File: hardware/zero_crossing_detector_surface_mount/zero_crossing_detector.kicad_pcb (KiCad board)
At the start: 2 copper layers, 93 x 61 mm, 98 parts, among them J1 Conn_01x02, J2 BOOT0, J3 Conn_02x15_Odd_Even, J4 USB_B_Micro, J6 K-Type, J7 BOOT1, Q1 2N3904, Q2 2N3904, Q3 2N3904, SW1 Reset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

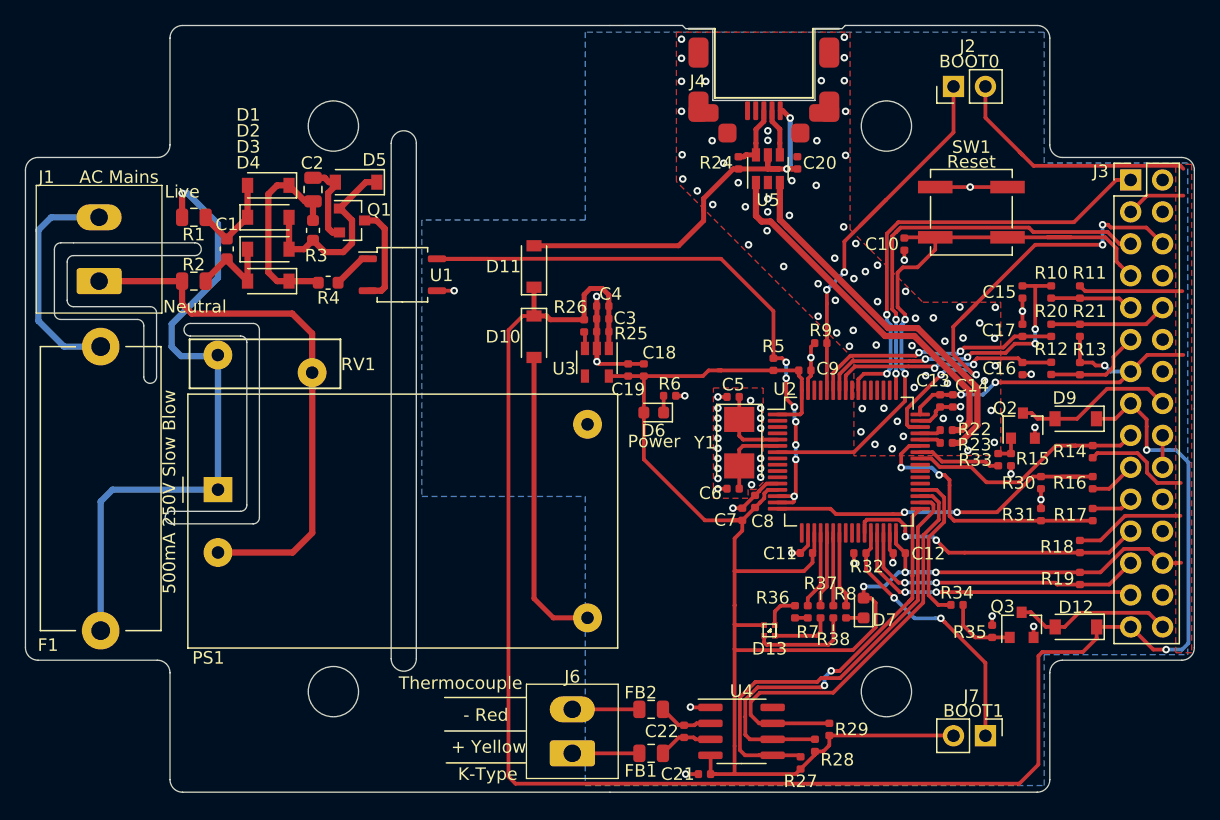
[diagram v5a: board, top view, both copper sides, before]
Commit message: Tweaked solder mask expansion
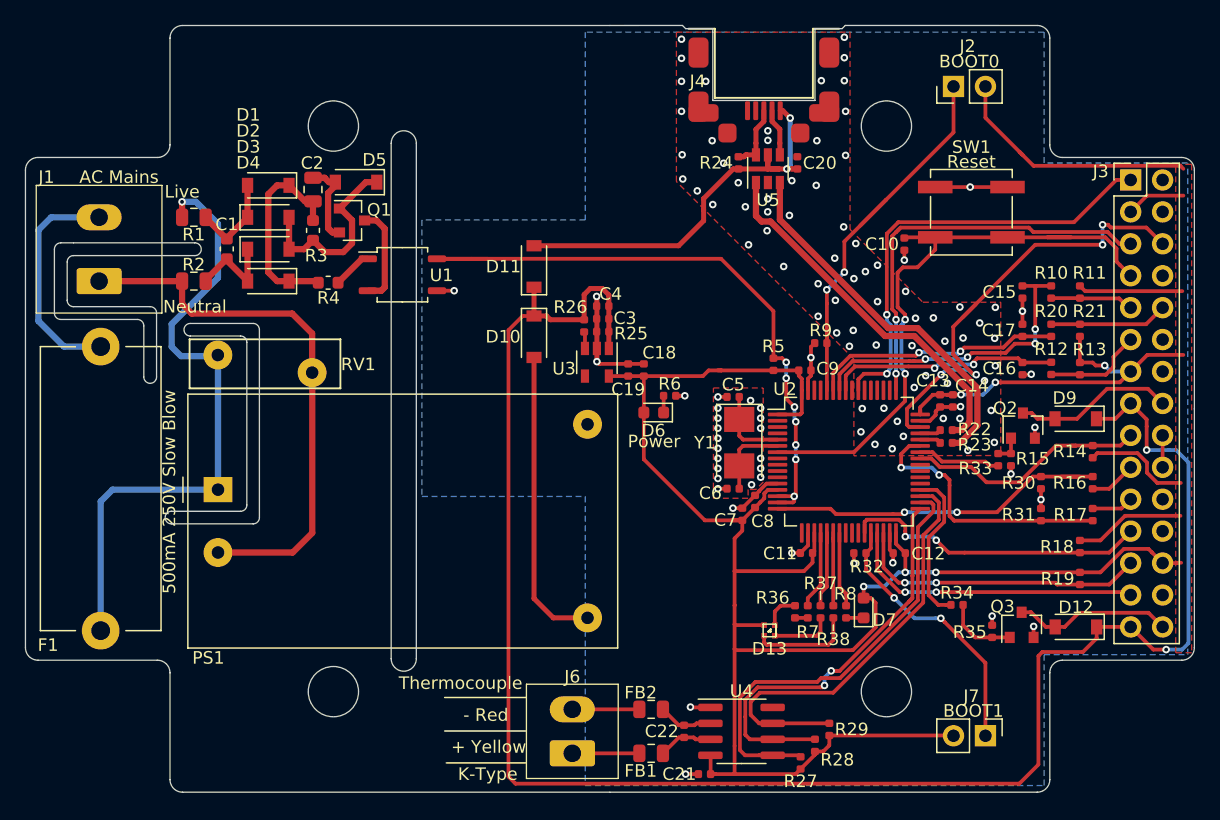
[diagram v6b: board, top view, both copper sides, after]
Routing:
- net /Fused_LIVE: track 51.7 -> 50.7 mm
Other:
- rule solder_mask_min_width: 0.25 -> 0.1
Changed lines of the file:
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@@
     (thickness 1.6)
     (drawings 147)
-    (tracks 912)
+    (tracks 913)
     (zones 0)
     (modules 98)
@@
   )
   (setup
-    (last_trace_width 0.4)
+    (last_trace_width 0.127)
     (user_trace_width 0.3)
     (user_trace_width 0.4)
@@
     (pad_drill 1)
     (pad_to_mask_clearance 0.051)
-    (solder_mask_min_width 0.25)
+    (solder_mask_min_width 0.1)
     (aux_axis_origin 0 0)
     (visible_elements FFFFFF7F)
@@
     (tags resistor)
     (attr smd)
-    (fp_text reference R33 (at 0.023 1.8288 180) (layer F.SilkS)
+    (fp_text reference R33 (at 0.6961 1.8161 180) (layer F.SilkS)
       (effects (font (size 1 1) (thickness 0.15)))
     )
@@
     (tags capacitor)
     (attr smd)
-    (fp_text reference C21 (at 2.136 0) (layer F.SilkS)
+    (fp_text reference C21 (at 2.009 0) (layer F.SilkS)
       (effects (font (size 1 1) (thickness 0.15)))
     )
@@
     (pad "" np_thru_hole circle (at 0 0) (size 4 4) (drill 4) (layers *.Cu *.Mask))
   )
+  (gr_text Live (at 175.964 52.728) (layer F.SilkS)
+    (effects (font (size 1 1) (thickness 0.15)))
+  )
   (gr_line (start 226.7585 85.1535) (end 226.7585 84.5185) (layer F.SilkS) (width 0.12))
   (gr_line (start 227.7745 87.63) (end 227.7745 87.1855) (layer F.SilkS) (width 0.12))
@@
     (effects (font (size 1 1) (thickness 0.15)))
   )
-  (gr_text Live (at 175.964 52.728) (layer F.SilkS)
-    (effects (font (size 1 1) (thickness 0.15)))
-  )
   (gr_arc (start 176 40.5) (end 176 39.5) (angle -90) (layer Edge.Cuts) (width 0.05))
   (gr_arc (start 174 49) (end 174 50) (angle -90) (layer Edge.Cuts) (width 0.05))
@@
     (effects (font (size 1.2 1.2) (thickness 0.2)) (justify mirror))
   )
-  (via (at 222.5675 48.641) (size 0.6) (drill 0.3) (layers F.Cu B.Cu) (net 5))
-  (via (at 222.5675 47.879) (size 0.6) (drill 0.3) (layers F.Cu B.Cu) (net 5))
-  (via (at 236.855 67.9704) (size 0.6) (drill 0.3) (layers F.Cu B.Cu) (net 5))
   (segment (start 177.839 54.806) (end 179.52 56.487) (width 0.5) (layer F.Cu) (net 1))
   (segment (start 177.839 54.76) (end 177.839 54.806) (width 0.5) (layer F.Cu) (net 1))
@@
   (segment (start 187.917 55.964) (end 187.579 55.626) (width 0.5) (layer F.Cu) (net 4))
   (segment (start 188.484 55.964) (end 187.917 55.964) (width 0.5) (layer F.Cu) (net 4))
+  (via (at 222.5675 48.641) (size 0.6) (drill 0.3) (layers F.Cu B.Cu) (net 5))
+  (via (at 222.5675 47.879) (size 0.6) (drill 0.3) (layers F.Cu B.Cu) (net 5))
+  (via (at 236.855 67.9704) (size 0.6) (drill 0.3) (layers F.Cu B.Cu) (net 5))
   (segment (start 220.5336 77.899) (end 221.5496 76.883) (width 0.3) (layer F.Cu) (net 5))
   (via (at 219.78684 77.9014) (size 0.6) (drill 0.3) (layers F.Cu B.Cu) (net 5))
@@
   (segment (start 170.423 76.43) (end 178.82 76.43) (width 0.5) (layer B.Cu) (net 37))
   (segment (start 169.487 77.366) (end 170.423 76.43) (width 0.5) (layer B.Cu) (net 37))
-  (via (at 175.964 52.855) (size 0.6) (drill 0.3) (layers F.Cu B.Cu) (net 37))
-  (segment (start 175.964 52.855) (end 175.964 54.76) (width 0.5) (layer F.Cu) (net 37))
-  (segment (start 176.388264 52.855) (end 178.816 55.282736) (width 0.5) (layer B.Cu) (net 37))
-  (segment (start 175.964 52.855) (end 176.388264 52.855) (width 0.5) (layer B.Cu) (net 37))
-  (segment (start 178.816 55.282736) (end 178.816 59.571) (width 0.5) (layer B.Cu) (net 37))
-  (segment (start 178.816 59.571) (end 175.133 63.254) (width 0.5) (layer B.Cu) (net 37))
-  (segment (start 175.133 63.254) (end 175.133 65.061) (width 0.5) (layer B.Cu) (net 37))
-  (segment (start 175.878 65.806) (end 178.82 65.806) (width 0.5) (layer B.Cu) (net 37))
-  (segment (start 175.133 65.061) (end 175.878 65.806) (width 0.5) (layer B.Cu) (net 37))
-  (segment (start 178.82 67.078792) (end 178.82 76.43) (width 0.5) (layer B.Cu) (net 37))
-  (segment (start 178.82 65.806) (end 178.82 67.078792) (width 0.5) (layer B.Cu) (net 37))
+  (segment (start 178.82 65.806) (end 175.878 65.806) (width 0.5) (layer B.Cu) (net 37))
+  (segment (start 175.878 65.806) (end 175.133 65.061) (width 0.5) (layer B.Cu) (net 37))
+  (segment (start 178.82 76.43) (end 178.82 65.806) (width 0.5) (layer B.Cu) (net 37))
+  (segment (start 175.133 65.061) (end 175.133 63.254) (width 0.5) (layer B.Cu) (net 37))
+  (segment (start 175.133 63.254) (end 178.816 59.571) (width 0.5) (layer B.Cu) (net 37))
+  (segment (start 178.816 59.571) (end 178.816 55.282736) (width 0.5) (layer B.Cu) (net 37))
+  (via (at 175.9585 53.5305) (size 0.6) (drill 0.3) (layers F.Cu B.Cu) (net 37))
+  (segment (start 175.964 54.76) (end 175.964 53.536) (width 0.5) (layer F.Cu) (net 37))
+  (segment (start 175.964 53.536) (end 175.9585 53.5305) (width 0.5) (layer F.Cu) (net 37))
+  (segment (start 177.063764 53.5305) (end 177.209632 53.676368) (width 0.5) (layer B.Cu) (net 37))
+  (segment (start 175.9585 53.5305) (end 177.063764 53.5305) (width 0.5) (layer B.Cu) (net 37))
+  (segment (start 178.816 55.282736) (end 177.209632 53.676368) (width 0.5) (layer B.Cu) (net 37))
   (segment (start 227.264 68.523) (end 227.264 66.892) (width 0.3) (layer F.Cu) (net 59))
   (segment (start 227.264 66.892) (end 227.264 64.77) (width 0.3) (layer F.Cu) (net 59))
@@
   (segment (start 222.9 47.131) (end 223.52004 47.75104) (width 0.4) (layer F.Cu) (net 61))
   (segment (start 222.9 46.281) (end 222.9 47.131) (width 0.4) (layer F.Cu) (net 61))
-  (segment (start 237.983962 71.6915) (end 237.2484 71.6915) (width 0.5) (layer F.Cu) (net 92))
-  (segment (start 238.611501 68.590787) (end 238.611501 71.063961) (width 0.5) (layer F.Cu) (net 92))
-  (segment (start 238.611501 71.063961) (end 237.983962 71.6915) (width 0.5) (layer F.Cu) (net 92))
-  (segment (start 222.075643 55.096043) (end 222.779957 55.096043) (width 0.5) (layer F.Cu) (net 92))
-  (segment (start 222.779957 55.096043) (end 231.888714 64.2048) (width 0.5) (layer F.Cu) (net 92))
-  (segment (start 234.225514 64.2048) (end 238.611501 68.590787) (width 0.5) (layer F.Cu) (net 92))
-  (segment (start 231.888714 64.2048) (end 234.225514 64.2048) (width 0.5) (layer F.Cu) (net 92))
-  (segment (start 237.854688 72.7075) (end 237.2484 72.7075) (width 0.5) (layer F.Cu) (net 91))
-  (segment (start 232.14843 63.57779) (end 234.48523 63.57779) (width 0.5) (layer F.Cu) (net 91))
-  (segment (start 239.238511 71.323677) (end 237.854688 72.7075) (width 0.5) (layer F.Cu) (net 91))
-  (segment (start 234.48523 63.57779) (end 239.23851 68.33107) (width 0.5) (layer F.Cu) (net 91))
-  (segment (start 239.23851 68.33107) (end 239.238511 71.323677) (width 0.5) (layer F.Cu) (net 91))
   (segment (start 230.764 81.0972) (end 230.378 81.4832) (width 0.3) (layer F.Cu) (net 62))
   (segment (start 230.764 79.873) (end 230.764 81.0972) (width 0.3) (layer F.Cu) (net 62))
@@
   (segment (start 227.764 80.317) (end 227.764 85.6615) (width 0.3) (layer F.Cu) (net 90))
   (segment (start 227.764 79.873) (end 227.764 80.317) (width 0.3) (layer F.Cu) (net 90))
+  (segment (start 237.854688 72.7075) (end 237.2484 72.7075) (width 0.5) (layer F.Cu) (net 91))
+  (segment (start 232.14843 63.57779) (end 234.48523 63.57779) (width 0.5) (layer F.Cu) (net 91))
+  (segment (start 239.238511 71.323677) (end 237.854688 72.7075) (width 0.5) (layer F.Cu) (net 91))
+  (segment (start 234.48523 63.57779) (end 239.23851 68.33107) (width 0.5) (layer F.Cu) (net 91))
+  (segment (start 239.23851 68.33107) (end 239.238511 71.323677) (width 0.5) (layer F.Cu) (net 91))
   (segment (start 223.52004 54.9494) (end 223.52004 51.99416) (width 0.5) (layer F.Cu) (net 91))
   (segment (start 224.07422 55.50358) (end 223.52004 54.9494) (width 0.5) (layer F.Cu) (net 91))
   (segment (start 224.07422 55.50358) (end 232.14843 63.57779) (width 0.5) (layer F.Cu) (net 91))
+  (segment (start 237.983962 71.6915) (end 237.2484 71.6915) (width 0.5) (layer F.Cu) (net 92))
+  (segment (start 238.611501 68.590787) (end 238.611501 71.063961) (width 0.5) (layer F.Cu) (net 92))
+  (segment (start 238.611501 71.063961) (end 237.983962 71.6915) (width 0.5) (layer F.Cu) (net 92))
+  (segment (start 222.075643 55.096043) (end 222.779957 55.096043) (width 0.5) (layer F.Cu) (net 92))
+  (segment (start 222.779957 55.096043) (end 231.888714 64.2048) (width 0.5) (layer F.Cu) (net 92))
+  (segment (start 234.225514 64.2048) (end 238.611501 68.590787) (width 0.5) (layer F.Cu) (net 92))
+  (segment (start 231.888714 64.2048) (end 234.225514 64.2048) (width 0.5) (layer F.Cu) (net 92))
   (segment (start 221.62004 54.60996) (end 221.62004 51.99416) (width 0.4) (layer F.Cu) (net 92))
   (segment (start 221.6048 54.6252) (end 221.62004 54.60996) (width 0.4) (layer F.Cu) (net 92))

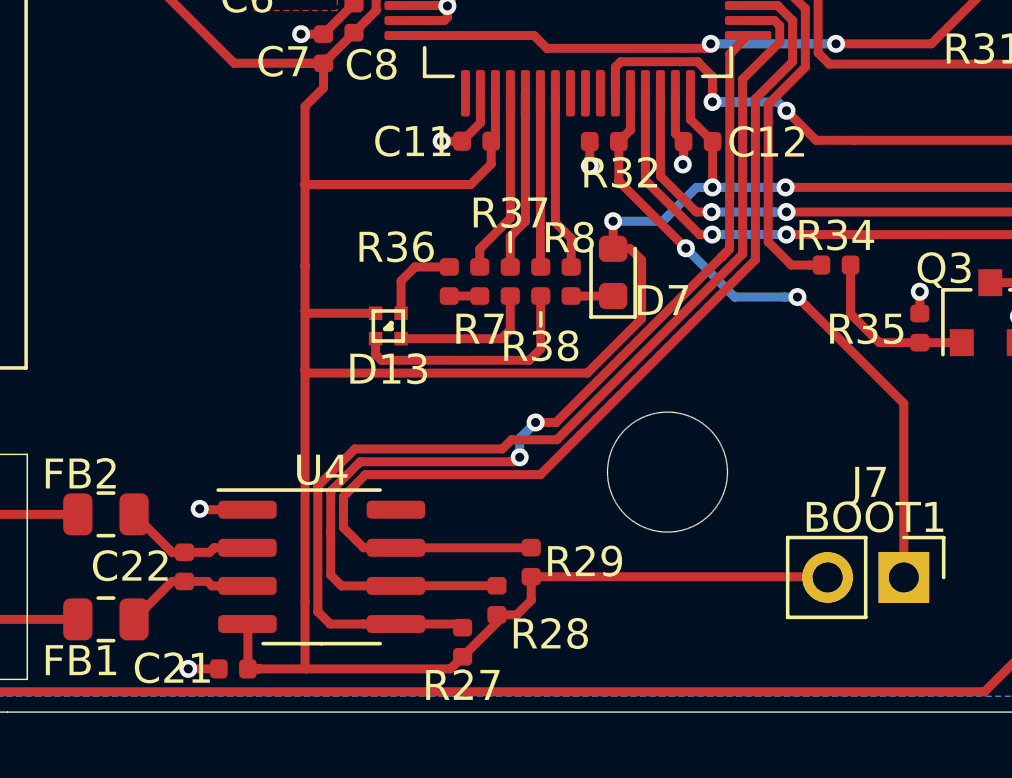
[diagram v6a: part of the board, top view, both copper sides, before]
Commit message: Rotated RGB led
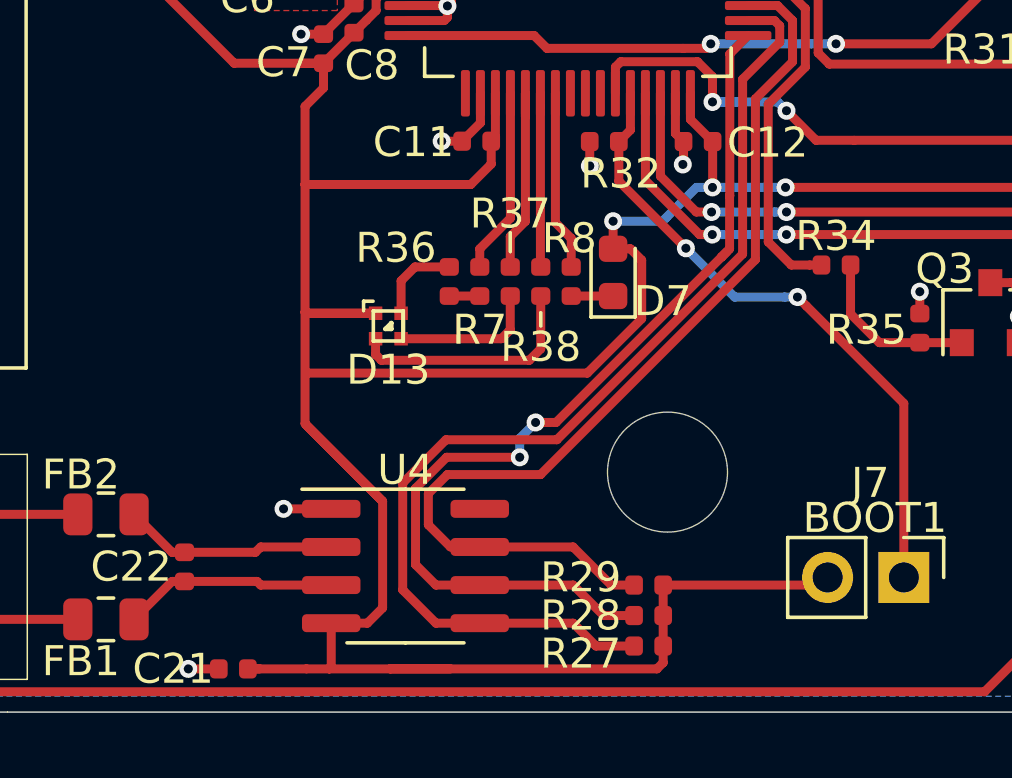
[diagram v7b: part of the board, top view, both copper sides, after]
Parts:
- moved R27 6.20 mm to (231.4, 98.3), turned to 0 degrees
- moved R28 5.08 mm to (231.4, 97.3), turned to 0 degrees
- moved R29 3.99 mm to (231.4, 96.3), turned to 0 degrees
- moved U4 2.79 mm to (223.3, 95.6)
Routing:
- net VCC: track 227.3 -> 236.9 mm
- net /T-: track 4.36 -> 7.17 mm
- net /T+: track 4.36 -> 7.15 mm
- net /MAX_MISO: track 34.7 -> 33.0 mm
- net /MAX_NSS: track 33.1 -> 32.3 mm

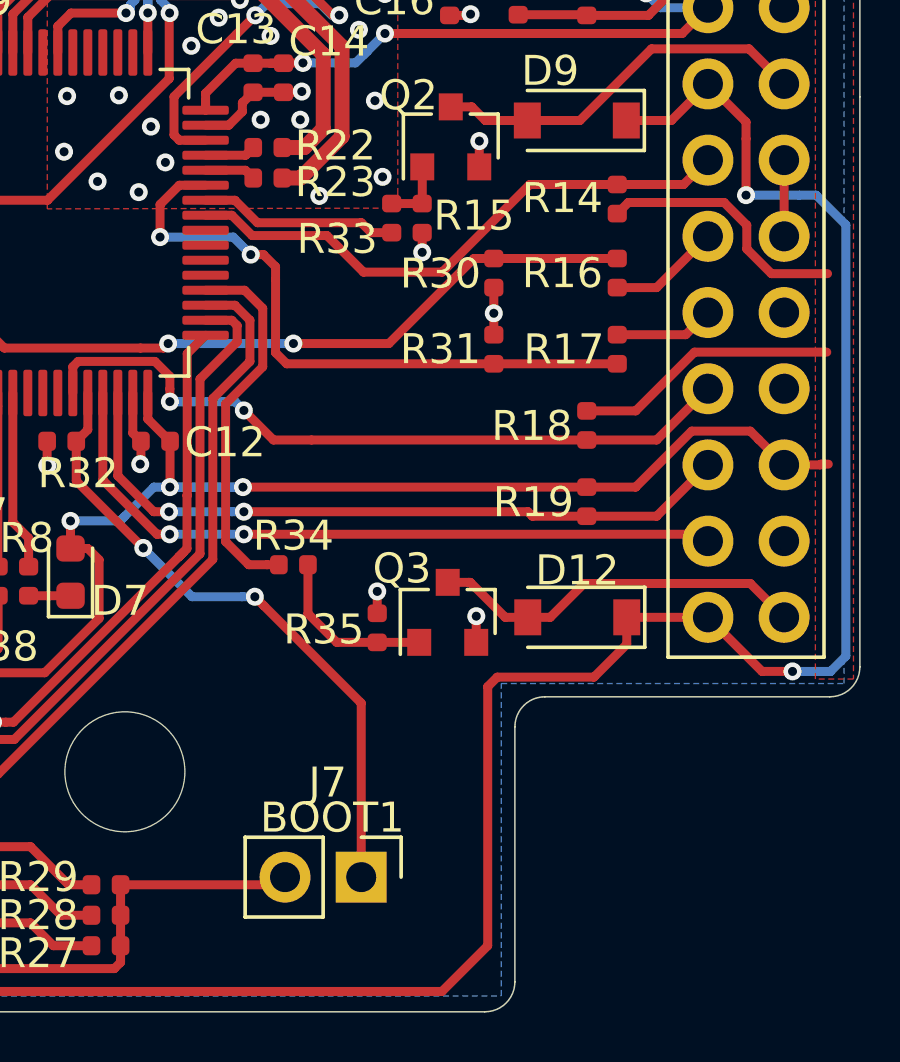
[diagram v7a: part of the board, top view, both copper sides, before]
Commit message: Added hw debouncing to trigger. Added SCL pull-up. Made both I2C pull-ups 2.2k and optional
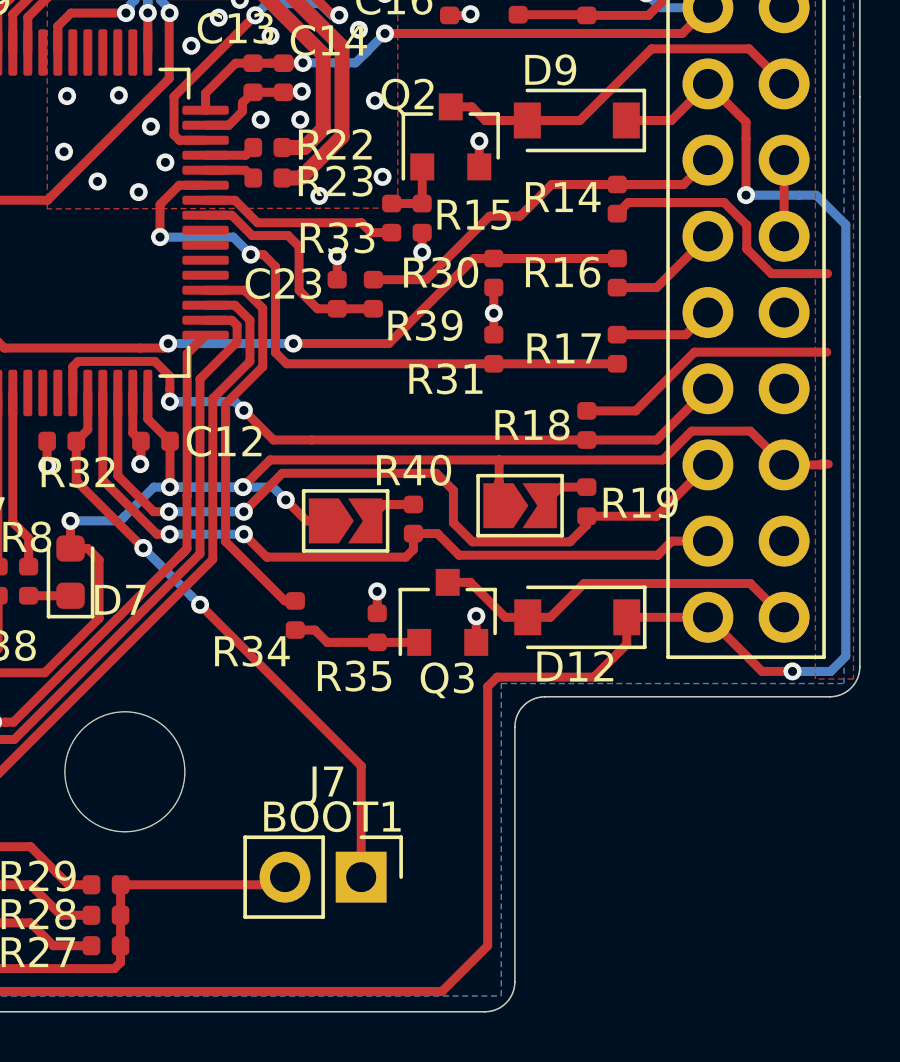
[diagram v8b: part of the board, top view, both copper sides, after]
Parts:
- added C23: 10nf, Capacitor_SMD:C_0402_1005Metric, F.Cu at (239.1, 76.6)
- added JP1: SolderJumper_2_Open, Jumper:SolderJumper-2_P1.3mm_Open_TrianglePad1.0x1.5mm, F.Cu at (239.4, 84.1)
- added JP2: SolderJumper_2_Open, Jumper:SolderJumper-2_P1.3mm_Open_TrianglePad1.0x1.5mm, F.Cu at (245.2, 83.6)
- added R39: 10k, Resistor_SMD:R_0402_1005Metric, F.Cu at (240.3, 76.6)
- added R40: 2.2k, Resistor_SMD:R_0402_1005Metric, F.Cu at (241.6, 84.1)
- R19: value 4.7k -> 2.2k
- moved R34 1.69 mm to (237.7, 87.3), turned to 90 degrees
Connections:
- J3 pad 17: /Trigger -> /Trigger_RAW
- R14 pad 1: /Trigger -> /Trigger_RAW
- R19 pad 1: VCC -> Net-(JP2-Pad2)
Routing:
- net /Trigger_RAW: track 0.00 -> 12.8 mm
- net /Trigger: track 19.4 -> 7.74 mm
- net VCC: track 236.9 -> 241.6 mm, vias 6 -> 7
- net /SDA: track 23.7 -> 26.3 mm
- net Net-(JP1-Pad2): track 0.00 -> 1.76 mm
- net Net-(JP2-Pad2): track 0.00 -> 1.75 mm
- net /SCL: track 24.0 -> 25.7 mm
- net Net-(Q3-Pad1): track 5.73 -> 4.30 mm
- net /BOOT1: track 21.5 -> 20.2 mm
- net /MISC: track 12.5 -> 13.6 mm
- net GND: track 54.9 -> 55.7 mm, vias 110 -> 111
